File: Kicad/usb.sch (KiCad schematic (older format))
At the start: 28 parts, among them J1001 USB Ports External, J1002 USB Ports Internal, U1001 AP2501, U1002 XR22404CG28, U1003 MIC2005A-2YM5, U1004 MIC2005A-2YM5, U1005 MIC2005A-2YM5, U1006 MIC2005A-2YM5, Y1001 12M

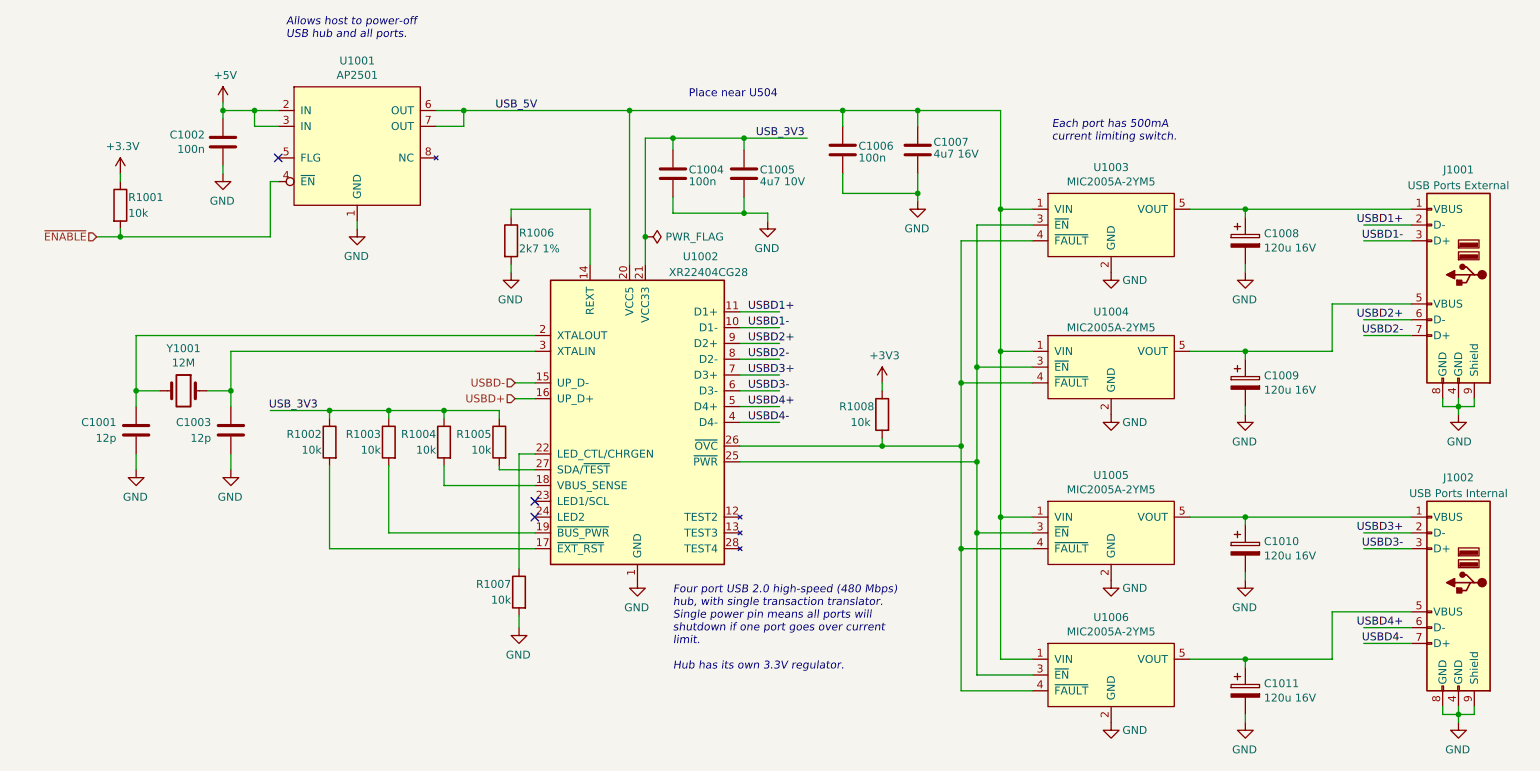
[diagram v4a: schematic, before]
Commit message: Tidy up part nos and swapped I2C/UART on BMC.
Mark all resistors as 1% if not specified.
Added some Mouser part numbers.
BMC can now be programmed over UART.
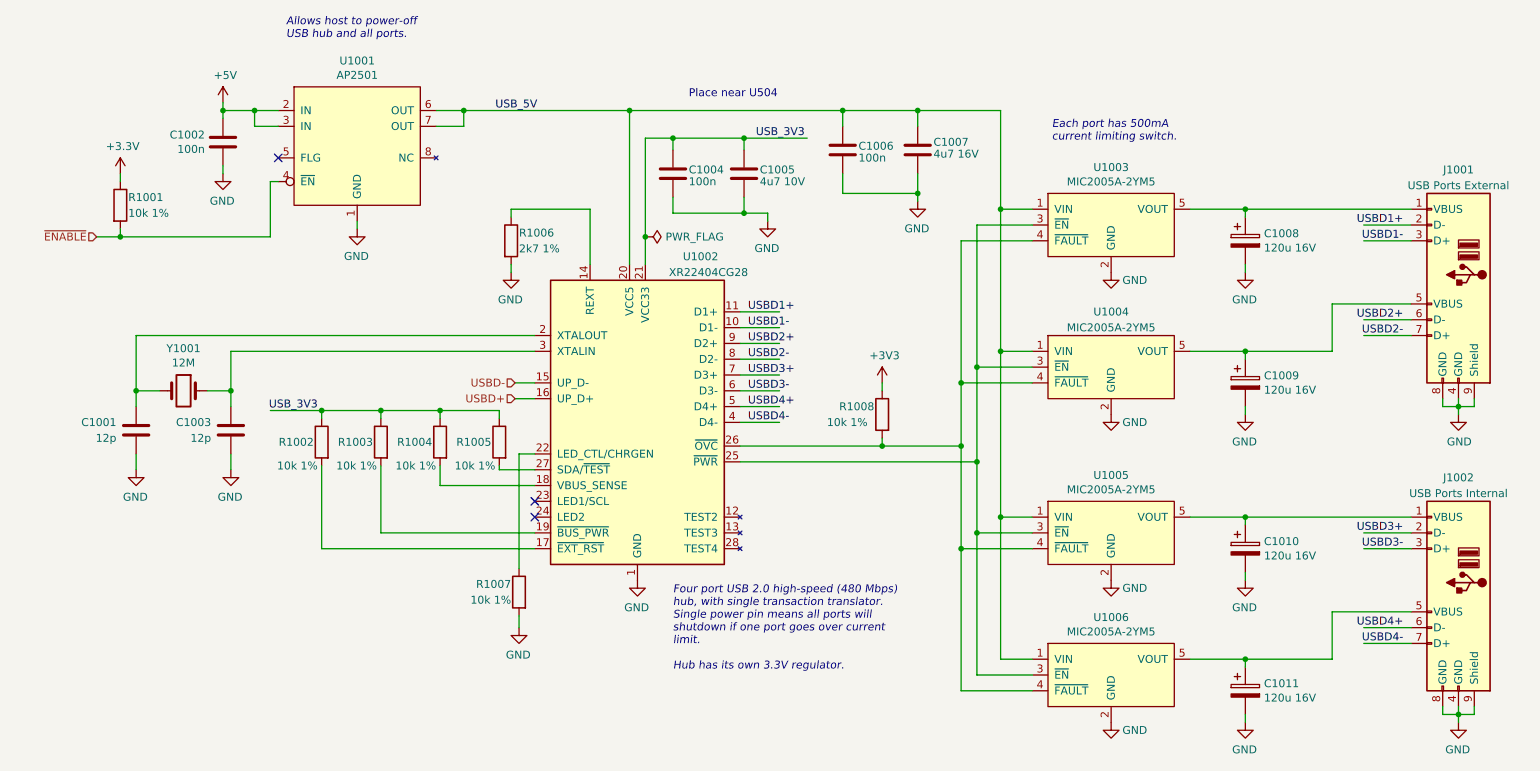
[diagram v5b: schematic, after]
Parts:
- C1002, C1004, C1006: Mouser (none) -> 594-K104K15X7RF5TL2
- C1008, C1009, C1010, C1011: Mouser (none) -> 647-UHE1C121MED
- J1001: Mouser (none) -> 490-UJ2-ADH-1-TH
- R1001, R1002, R1003, R1004, R1005, R1007, R1008: value 10k -> 10k 1%
- U1001: Mouser (none) -> 621-AP2501S-13
- U1003, U1004, U1005, U1006: Mouser (none) -> 998-MIC2005A-2YM5TR
- Y1001: Mouser (none) -> 815-ABL-12-B2
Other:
- moved on the sheet: R1002, R1003, R1004
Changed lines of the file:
@@
 F 6 "102-4001-ND" H 9925 3975 50  0001 C CNN "Digikey"
 F 7 "0" H 9925 2925 50  0001 C CNN "DNP"
+F 8 "490-UJ2-ADH-1-TH" H 9925 2925 50  0001 C CNN "Mouser"
 	1    9925 2925
 	-1   0    0    -1
@@
 F 6 "MIC2005A-2YM5" H 7725 2225 50  0001 C CNN "MPN"
 F 7 "Microchip" H 7725 2225 50  0001 C CNN "Manufacturer"
+F 8 "998-MIC2005A-2YM5TR" H 7725 2225 50  0001 C CNN "Mouser"
 	1    7725 2225
 	1    0    0    -1
@@
 F 6 "MIC2005A-2YM5" H 7725 3125 50  0001 C CNN "MPN"
 F 7 "Microchip" H 7725 3125 50  0001 C CNN "Manufacturer"
+F 8 "998-MIC2005A-2YM5TR" H 7725 3125 50  0001 C CNN "Mouser"
 	1    7725 3125
 	1    0    0    -1
@@
 P 6275 3425
 F 0 "R1008" H 6325 3475 50  0000 L CNN
-F 1 "10k" H 6475 3375 50  0000 R CNN
+F 1 "10k 1%" H 6625 3375 50  0000 R CNN
 F 2 "Resistor_SMD:R_0805_2012Metric_Pad1.20x1.40mm_HandSolder" V 6205 3425 50  0001 C CNN
 F 3 "~" H 6275 3425 50  0001 C CNN
@@
 F 6 "MIC2005A-2YM5" H 7725 4175 50  0001 C CNN "MPN"
 F 7 "Microchip" H 7725 4175 50  0001 C CNN "Manufacturer"
+F 8 "998-MIC2005A-2YM5TR" H 7725 4175 50  0001 C CNN "Mouser"
 	1    7725 4175
 	1    0    0    -1
@@
 F 6 "MIC2005A-2YM5" H 7725 5075 50  0001 C CNN "MPN"
 F 7 "Microchip" H 7725 5075 50  0001 C CNN "Manufacturer"
+F 8 "998-MIC2005A-2YM5TR" H 7725 5075 50  0001 C CNN "Mouser"
 	1    7725 5075
 	1    0    0    -1
@@
 F 6 "ABL-12.000MHZ-B2" H 1850 3275 50  0001 C CNN "MPN"
 F 7 "Abracon" H 1850 3275 50  0001 C CNN "Manufacturer"
+F 8 "815-ABL-12-B2" H 1850 3275 50  0001 C CNN "Mouser"
 	1    1850 3275
 	-1   0    0    -1
@@
 F 6 "K104K15X7RF5TL2" H 6025 1750 50  0001 C CNN "MPN"
 F 7 "Vishay" H 6025 1750 50  0001 C CNN "Manufacturer"
+F 8 "594-K104K15X7RF5TL2" H 6025 1750 50  0001 C CNN "Mouser"
 	1    6025 1750
 	1    0    0    -1
@@
 F 6 "UHE1C121MED" H 8575 2325 50  0001 C CNN "MPN"
 F 7 "Nichicon" H 8575 2325 50  0001 C CNN "Manufacturer"
+F 8 "647-UHE1C121MED" H 8575 2325 50  0001 C CNN "Mouser"
 	1    8575 2325
 	1    0    0    -1
@@
 F 6 "UHE1C121MED" H 8575 3225 50  0001 C CNN "MPN"
 F 7 "Nichicon" H 8575 3225 50  0001 C CNN "Manufacturer"
+F 8 "647-UHE1C121MED" H 8575 3225 50  0001 C CNN "Mouser"
 	1    8575 3225
 	1    0    0    -1
@@
 F 6 "UHE1C121MED" H 8575 4275 50  0001 C CNN "MPN"
 F 7 "Nichicon" H 8575 4275 50  0001 C CNN "Manufacturer"
+F 8 "647-UHE1C121MED" H 8575 4275 50  0001 C CNN "Mouser"
 	1    8575 4275
 	1    0    0    -1
@@
 F 6 "UHE1C121MED" H 8575 5175 50  0001 C CNN "MPN"
 F 7 "Nichicon" H 8575 5175 50  0001 C CNN "Manufacturer"
+F 8 "647-UHE1C121MED" H 8575 5175 50  0001 C CNN "Mouser"
 	1    8575 5175
 	1    0    0    -1
@@
 L Device:R R1002
 U 1 1 5FF19ACF
-P 2775 3600
-F 0 "R1002" H 2825 3650 50  0000 L CNN
-F 1 "10k" H 2825 3550 50  0000 L CNN
-F 2 "Resistor_SMD:R_0805_2012Metric_Pad1.20x1.40mm_HandSolder" V 2705 3600 50  0001 C CNN
-F 3 "~" H 2775 3600 50  0001 C CNN
-F 4 "0" H 2775 3600 50  0001 C CNN "DNP"
-F 5 "RMCF0805FT10K0-ND" H 2775 3600 50  0001 C CNN "Digikey"
-F 6 "RMCF0805FT10K0" H 2775 3600 50  0001 C CNN "MPN"
-F 7 "Stackpole" H 2775 3600 50  0001 C CNN "Manufacturer"
-	1    2775 3600
+P 2725 3600
+F 0 "R1002" H 2775 3600 50  0000 L CNN
+F 1 "10k 1%" H 2750 3450 50  0000 L CNN
+F 2 "Resistor_SMD:R_0805_2012Metric_Pad1.20x1.40mm_HandSolder" V 2655 3600 50  0001 C CNN
+F 3 "~" H 2725 3600 50  0001 C CNN
+F 4 "0" H 2725 3600 50  0001 C CNN "DNP"
+F 5 "RMCF0805FT10K0-ND" H 2725 3600 50  0001 C CNN "Digikey"
+F 6 "RMCF0805FT10K0" H 2725 3600 50  0001 C CNN "MPN"
+F 7 "Stackpole" H 2725 3600 50  0001 C CNN "Manufacturer"
+	1    2725 3600
 	-1   0    0    -1
 $EndComp
@@
 P 3975 4550
 F 0 "R1007" H 4025 4600 50  0000 L CNN
-F 1 "10k" H 4025 4500 50  0000 L CNN
+F 1 "10k 1%" H 4025 4500 50  0000 L CNN
 F 2 "Resistor_SMD:R_0805_2012Metric_Pad1.20x1.40mm_HandSolder" V 3905 4550 50  0001 C CNN
 F 3 "~" H 3975 4550 50  0001 C CNN
@@
 F 6 "0" H 2950 750 50  0001 C CNN "DNP"
 F 7 "AP2501S-13DICT-ND" H 2950 750 50  0001 C CNN "Digikey"
+F 8 "621-AP2501S-13" H 2950 750 50  0001 C CNN "Mouser"
 	1    2950 750
 	1    0    0    -1
@@
 P 1450 2100
 F 0 "R1001" H 1500 2150 50  0000 L CNN
-F 1 "10k" H 1500 2050 50  0000 L CNN
+F 1 "10k 1%" H 1500 2050 50  0000 L CNN
 F 2 "Resistor_SMD:R_0805_2012Metric_Pad1.20x1.40mm_HandSolder" V 1380 2100 50  0001 C CNN
 F 3 "~" H 1450 2100 50  0001 C CNN
@@
 F 6 "K104K15X7RF5TL2" H 2100 1700 50  0001 C CNN "MPN"
 F 7 "Vishay" H 2100 1700 50  0001 C CNN "Manufacturer"
+F 8 "594-K104K15X7RF5TL2" H 2100 1700 50  0001 C CNN "Mouser"
 	1    2100 1700
 	-1   0    0    -1
@@
 U 1 1 5FF91B12
 P 3850 3600
-F 0 "R1005" H 3900 3650 50  0000 L CNN
-F 1 "10k" H 3900 3550 50  0000 L CNN
+F 0 "R1005" H 3900 3600 50  0000 L CNN
+F 1 "10k 1%" H 3875 3450 50  0000 L CNN
 F 2 "Resistor_SMD:R_0805_2012Metric_Pad1.20x1.40mm_HandSolder" V 3780 3600 50  0001 C CNN
 F 3 "~" H 3850 3600 50  0001 C CNN
@@
 L Device:R R1004
 U 1 1 5FF9224A
-P 3500 3600
-F 0 "R1004" H 3550 3650 50  0000 L CNN
-F 1 "10k" H 3550 3550 50  0000 L CNN
-F 2 "Resistor_SMD:R_0805_2012Metric_Pad1.20x1.40mm_HandSolder" V 3430 3600 50  0001 C CNN
-F 3 "~" H 3500 3600 50  0001 C CNN
-F 4 "0" H 3500 3600 50  0001 C CNN "DNP"
-F 5 "RMCF0805FT10K0-ND" H 3500 3600 50  0001 C CNN "Digikey"
-F 6 "RMCF0805FT10K0" H 3500 3600 50  0001 C CNN "MPN"
-F 7 "Stackpole" H 3500 3600 50  0001 C CNN "Manufacturer"
-	1    3500 3600
+P 3475 3600
+F 0 "R1004" H 3525 3600 50  0000 L CNN
+F 1 "10k 1%" H 3500 3450 50  0000 L CNN
+F 2 "Resistor_SMD:R_0805_2012Metric_Pad1.20x1.40mm_HandSolder" V 3405 3600 50  0001 C CNN
+F 3 "~" H 3475 3600 50  0001 C CNN
+F 4 "0" H 3475 3600 50  0001 C CNN "DNP"
+F 5 "RMCF0805FT10K0-ND" H 3475 3600 50  0001 C CNN "Digikey"
+F 6 "RMCF0805FT10K0" H 3475 3600 50  0001 C CNN "MPN"
+F 7 "Stackpole" H 3475 3600 50  0001 C CNN "Manufacturer"
+	1    3475 3600
 	-1   0    0    -1
 $EndComp
@@
 L Device:R R1003
 U 1 1 5FF92655
-P 3150 3600
-F 0 "R1003" H 3200 3650 50  0000 L CNN
-F 1 "10k" H 3200 3550 50  0000 L CNN
-F 2 "Resistor_SMD:R_0805_2012Metric_Pad1.20x1.40mm_HandSolder" V 3080 3600 50  0001 C CNN
-F 3 "~" H 3150 3600 50  0001 C CNN
-F 4 "0" H 3150 3600 50  0001 C CNN "DNP"
-F 5 "RMCF0805FT10K0-ND" H 3150 3600 50  0001 C CNN "Digikey"
-F 6 "RMCF0805FT10K0" H 3150 3600 50  0001 C CNN "MPN"
-F 7 "Stackpole" H 3150 3600 50  0001 C CNN "Manufacturer"
-	1    3150 3600
+P 3100 3600
+F 0 "R1003" H 3150 3600 50  0000 L CNN
+F 1 "10k 1%" H 3125 3450 50  0000 L CNN
+F 2 "Resistor_SMD:R_0805_2012Metric_Pad1.20x1.40mm_HandSolder" V 3030 3600 50  0001 C CNN
+F 3 "~" H 3100 3600 50  0001 C CNN
+F 4 "0" H 3100 3600 50  0001 C CNN "DNP"
+F 5 "RMCF0805FT10K0-ND" H 3100 3600 50  0001 C CNN "Digikey"
+F 6 "RMCF0805FT10K0" H 3100 3600 50  0001 C CNN "MPN"
+F 7 "Stackpole" H 3100 3600 50  0001 C CNN "Manufacturer"
+	1    3100 3600
 	-1   0    0    -1
 $EndComp
@@
 	2150 3025 4075 3025
 Wire Wire Line
-	3150 3400 3150 3450
-Wire Wire Line
-	3150 3400 3500 3400
-Wire Wire Line
-	3500 3400 3500 3450
-Connection ~ 3150 3400
-Wire Wire Line
-	3500 3400 3850 3400
+	3100 3400 3100 3450
+Wire Wire Line
+	3475 3400 3475 3450
+Wire Wire Line
+	3475 3400 3850 3400
 Wire Wire Line
 	3850 3400 3850 3450
-Connection ~ 3500 3400
+Connection ~ 3475 3400
 Wire Wire Line
 	3850 3775 4075 3775
@@
 	3850 3775 3850 3750
 Wire Wire Line
-	2775 3400 3150 3400
-Wire Wire Line
-	2400 3400 2775 3400
-Connection ~ 2775 3400
-Wire Wire Line
-	4075 3875 3500 3875
-Wire Wire Line
-	3500 3875 3500 3750
-Wire Wire Line
-	3150 4175 3150 3750
-Wire Wire Line
-	3150 4175 4075 4175
-Wire Wire Line
-	2775 4275 2775 3750
-Wire Wire Line
-	2775 4275 4075 4275
-Wire Wire Line
-	2775 3400 2775 3450
+	3475 3875 3475 3750
+Wire Wire Line
+	3100 4175 3100 3750
+Wire Wire Line
+	2725 4275 2725 3750
+Wire Wire Line
+	2725 3400 2725 3450
 $Comp
 L Device:C C1004
@@
 F 6 "K104K15X7RF5TL2" H 4950 1900 50  0001 C CNN "MPN"
 F 7 "Vishay" H 4950 1900 50  0001 C CNN "Manufacturer"
+F 8 "594-K104K15X7RF5TL2" H 4950 1900 50  0001 C CNN "Mouser"
 	1    4950 1900
 	1    0    0    -1
@@
 	5550 2150 5550 2200
 Connection ~ 5400 2150
+Connection ~ 3100 3400
+Wire Wire Line
+	3100 3400 3475 3400
+Wire Wire Line
+	3100 4175 4075 4175
+Wire Wire Line
+	3475 3875 4075 3875
+Connection ~ 2725 3400
+Wire Wire Line
+	2725 3400 3100 3400
+Wire Wire Line
+	2725 4275 4075 4275
+Wire Wire Line
+	2400 3400 2725 3400
 $EndSCHEMATC

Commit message: Changes to BMC
* Swapped BUTTON_PWR and SYS_RESET to avoid DRC issue
* Split PSU and BMC into two separate sheets
* Swapped some pins on the STM32 to make it compatible with more
alternatives
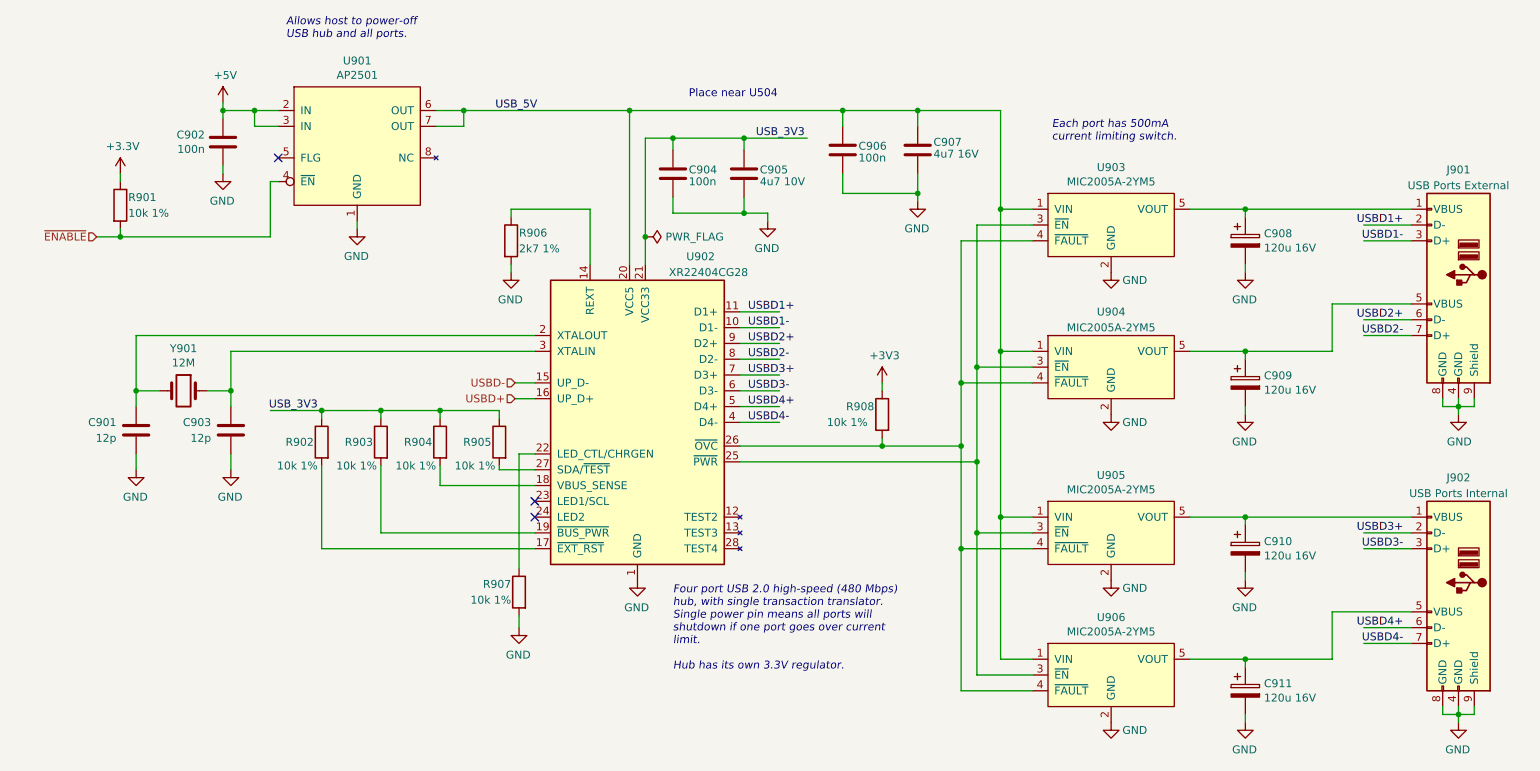
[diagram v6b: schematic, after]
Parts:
- renumbered C1001 to C901, C1002 to C902, C1003 to C903, C1004 to C904, C1005 to C905, C1006 to C906, C1007 to C907, C1008 to C908, C1009 to C909, C1010 to C910, C1011 to C911, J1001 to J901, J1002 to J902, R1001 to R901, R1002 to R902, R1003 to R903, R1004 to R904, R1005 to R905, R1006 to R906, R1007 to R907, R1008 to R908, U1001 to U901, U1002 to U902, U1003 to U903, U1004 to U904, U1005 to U905, U1006 to U906, Y1001 to Y901
